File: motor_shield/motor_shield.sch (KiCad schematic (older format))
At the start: 22 parts, among them J1 Screw_Terminal_01x02, J2 Screw_Terminal_01x02, J3 Screw_Terminal_01x02, J4 Conn_01x04, J5 Conn_01x04, J6 Conn_01x04, U1 DRV8834_CARRIER, U10 SHARP_GP2Y0A21YK0F, U11 SHARP_GP2Y0A21YK0F, U2 DRV8834_CARRIER, U3 DRV8834_CARRIER, U4 ARDUINO_MICRO, U5 RASPBERRY_PI, U6 SHARP_GP2Y0A21YK0F, U7 SHARP_GP2Y0A21YK0F, U8 SHARP_GP2Y0A21YK0F, U9 SHARP_GP2Y0A21YK0F

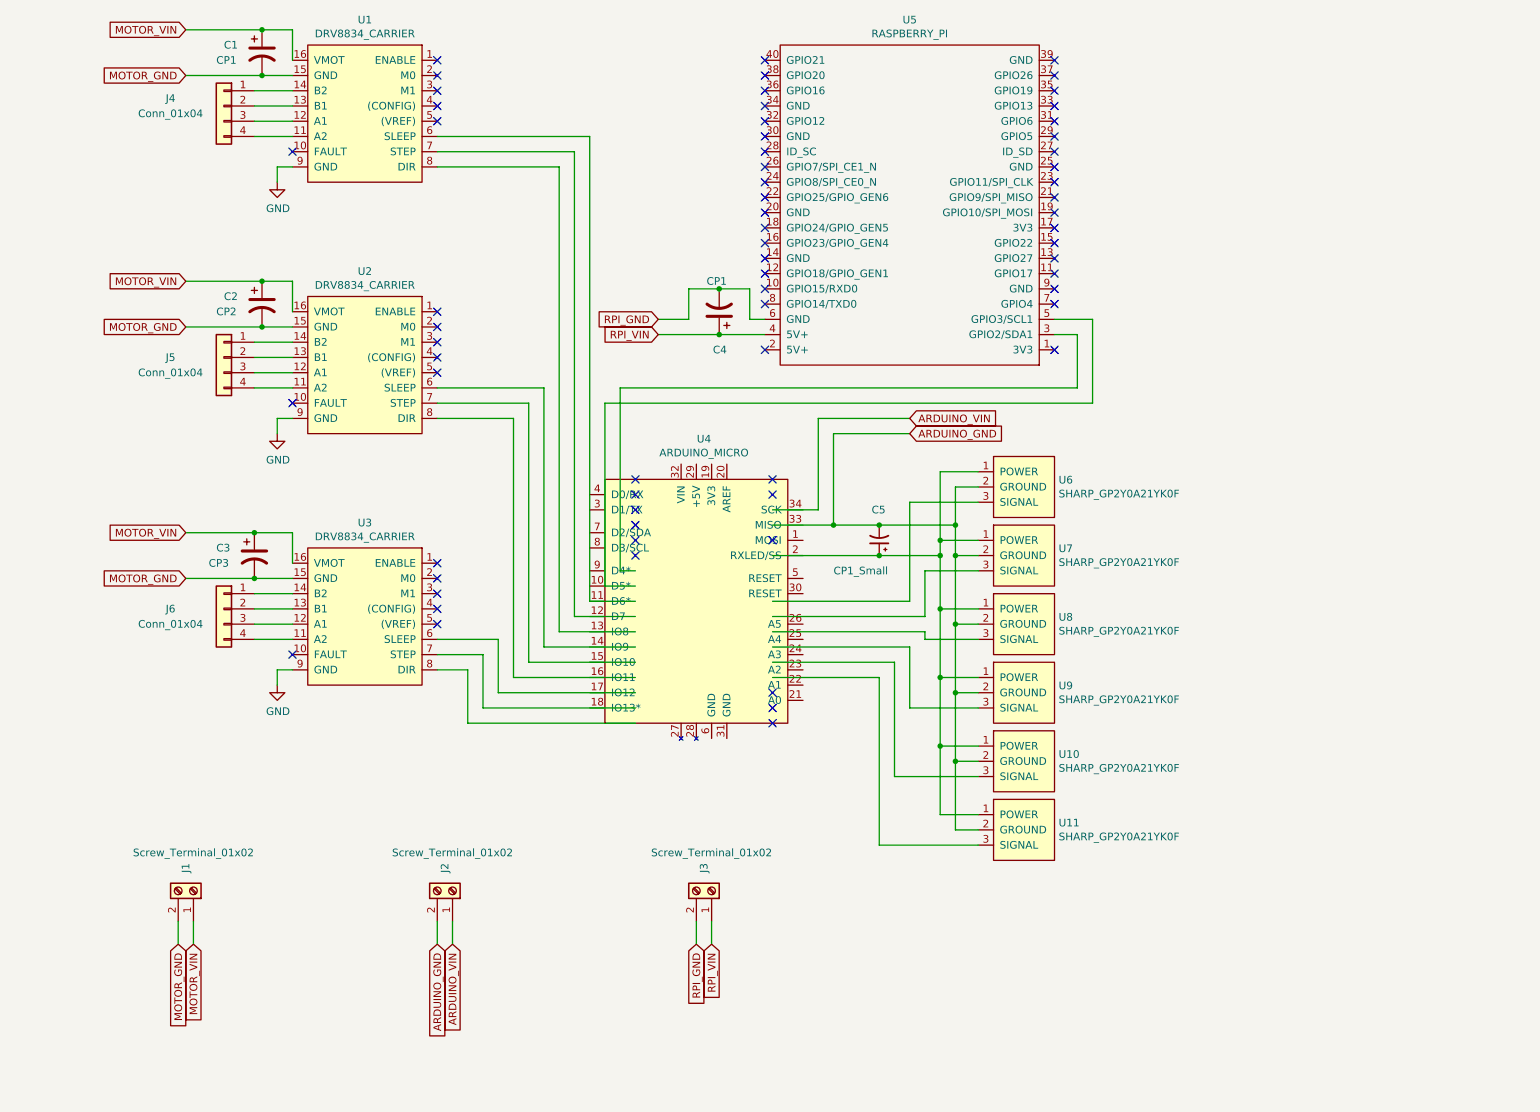
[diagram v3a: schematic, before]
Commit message: Continued work on motor shield
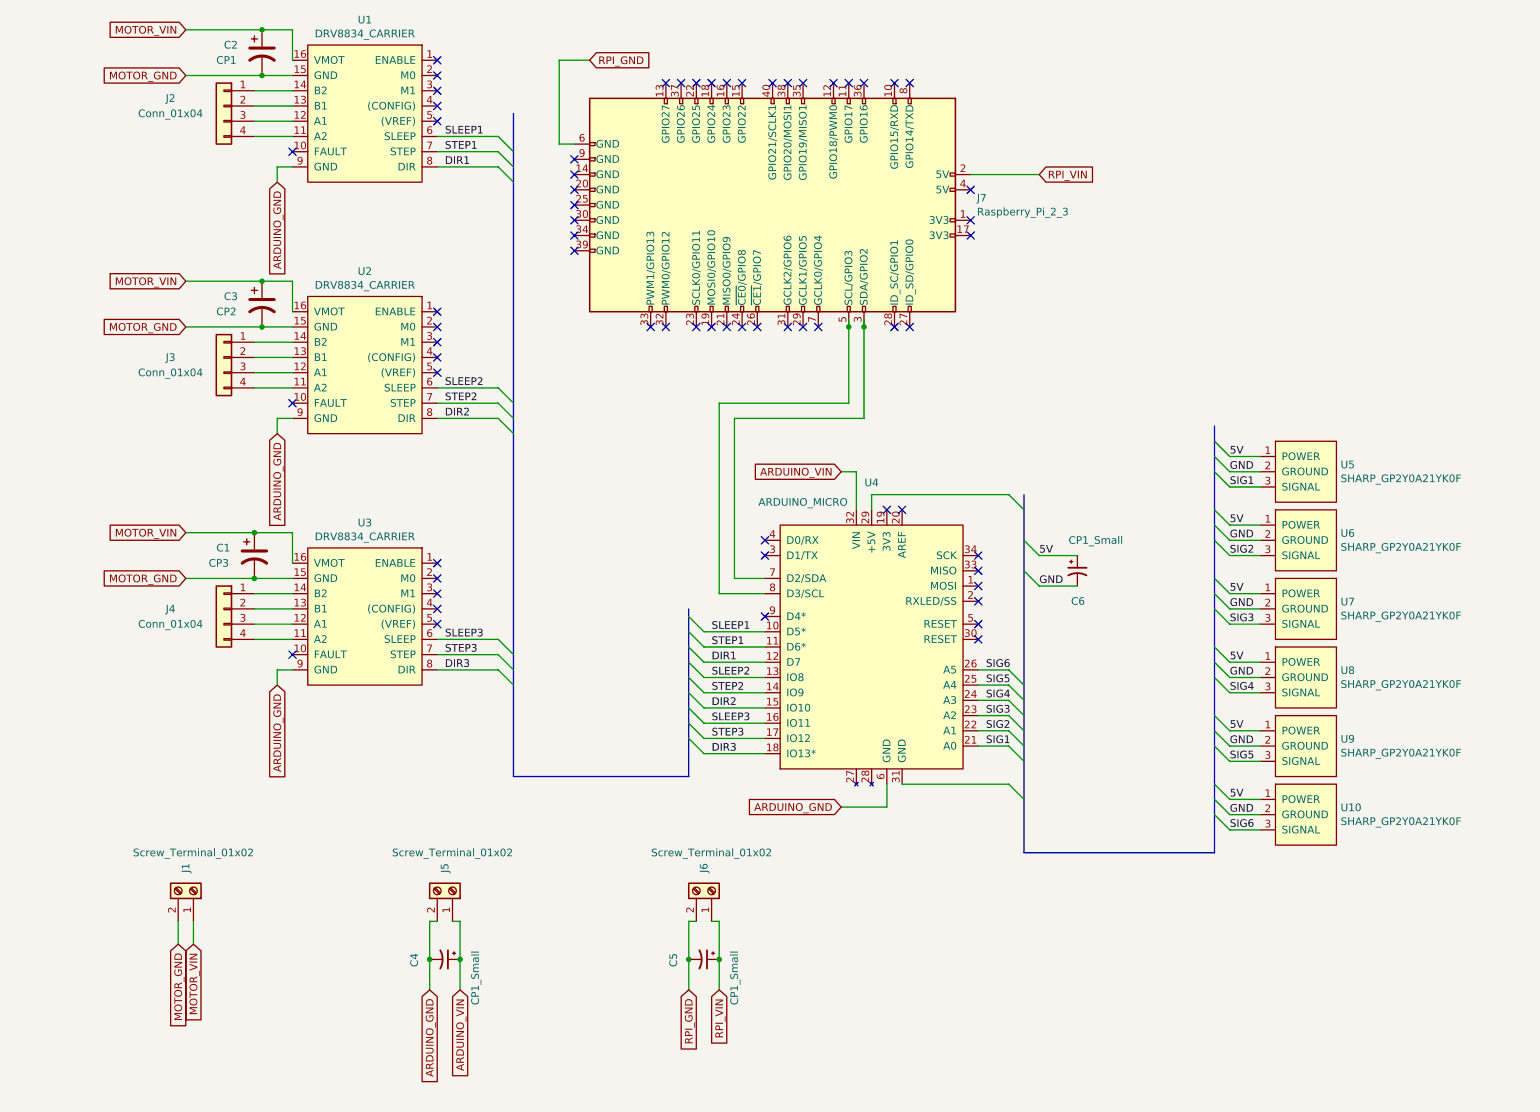
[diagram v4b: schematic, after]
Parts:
- removed C4: CP1, Capacitor_THT:CP_Radial_D8.0mm_P2.50mm, symbol Device:CP1
- removed U5: RASPBERRY_PI, Connector_PinHeader_2.54mm:PinHeader_2x20_P2.54mm_Vertical, symbol CATPOO:RASPBERRY_PI
- added C5, C6: CP1_Small, Capacitor_THT:CP_Radial_D5.0mm_P2.50mm, symbol Device:CP1_Small
- added J7: Raspberry_Pi_2_3, Connector_PinHeader_2.54mm:PinHeader_2x20_P2.54mm_Vertical, symbol Connector:Raspberry_Pi_2_3
- renumbered C3 to C1, C1 to C2, C2 to C3, C5 to C4, J4 to J2, J5 to J3, J6 to J4, J2 to J5, J3 to J6, U11 to U10, U6 to U5, U7 to U6, U8 to U7, U9 to U8, U10 to U9
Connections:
- net labels added: 5V, DIR1, DIR2, DIR3, SIG1, SIG2, SIG3, SIG4, SIG5, SIG6, SLEEP1, SLEEP2, SLEEP3, STEP1, STEP2, STEP3
- wire segments 136 -> 112
- no-connect marks 66 -> 65
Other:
- moved on the sheet: C4, U10, U5, U6, U7, U8, U9

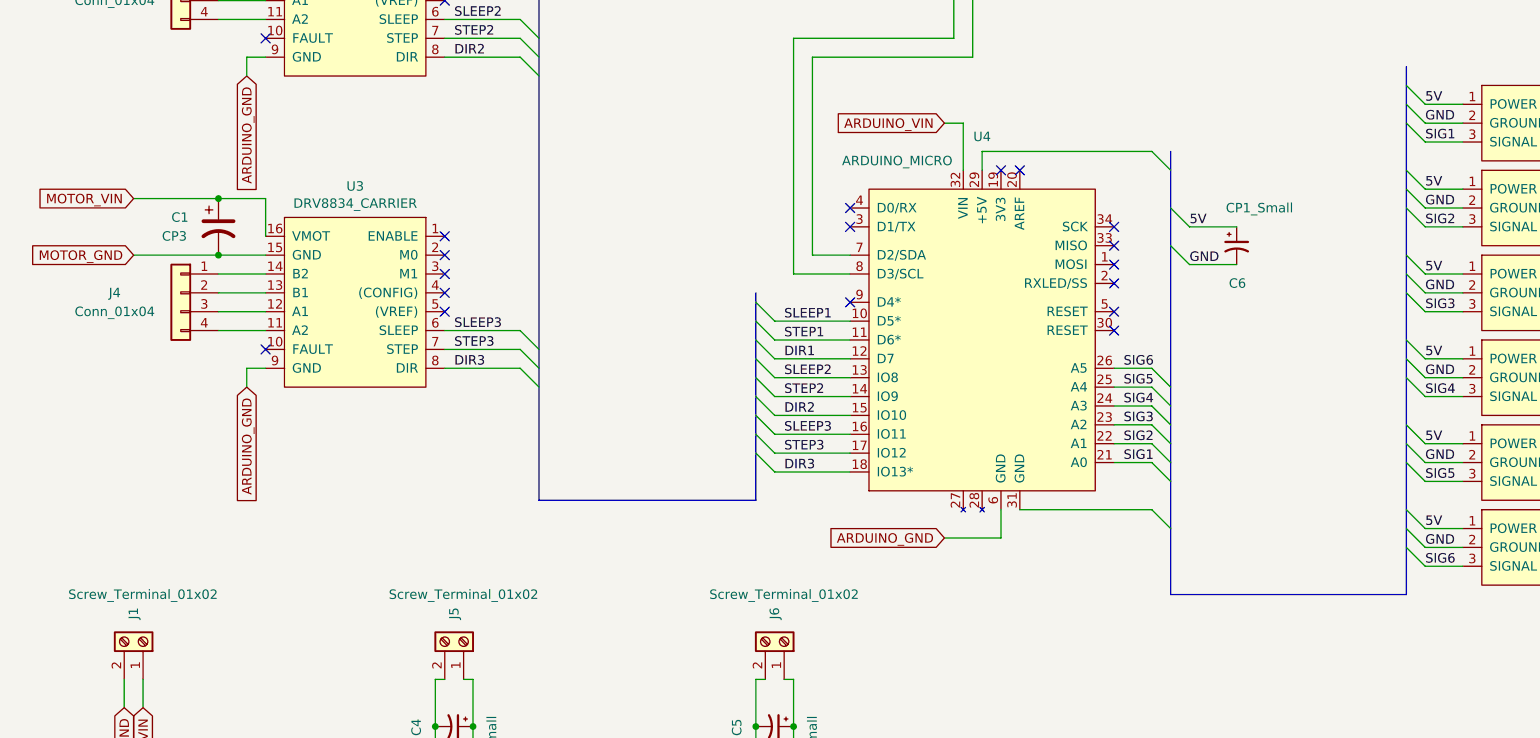
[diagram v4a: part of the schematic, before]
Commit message: Fix mobo schematic
flipped the order of dir, step, sleep to make it easier to route wires
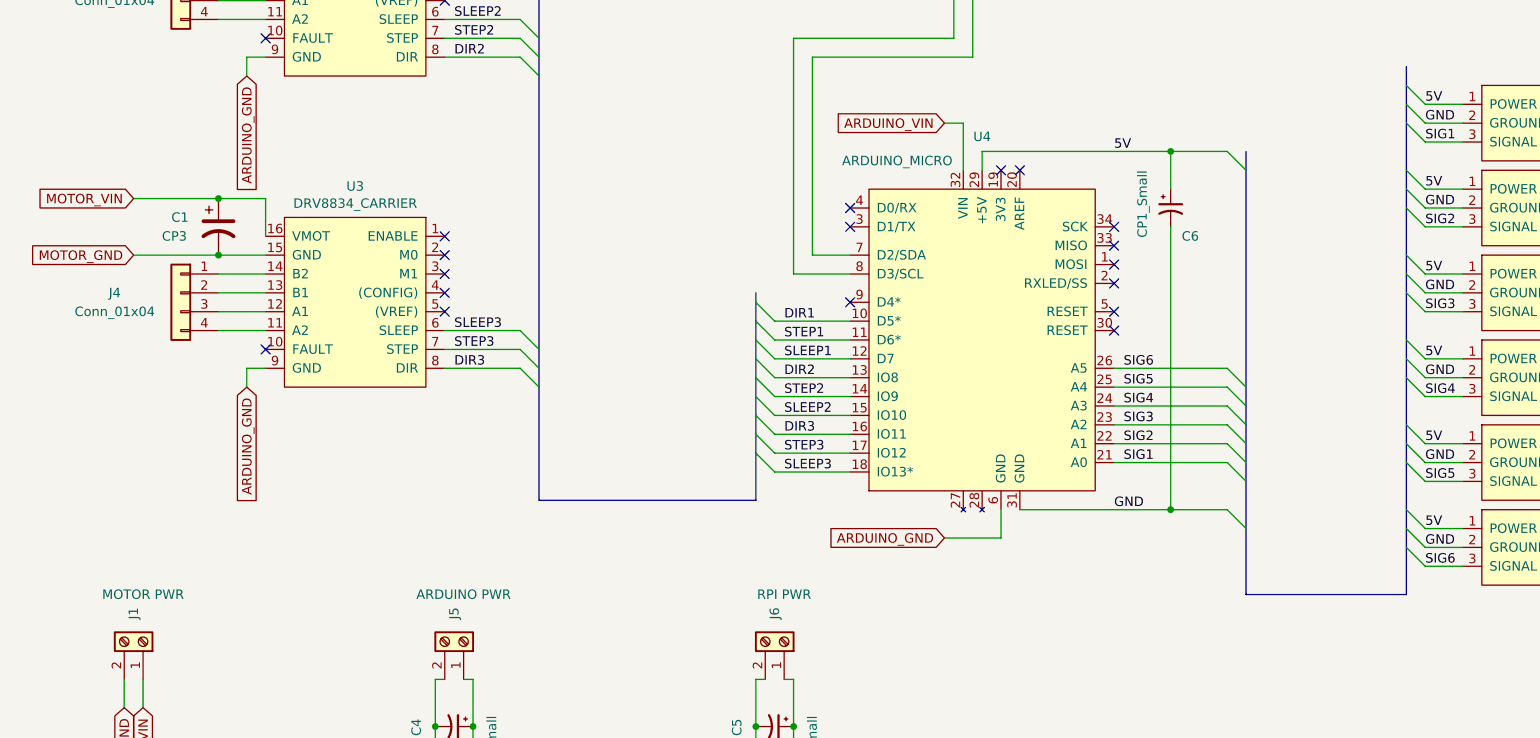
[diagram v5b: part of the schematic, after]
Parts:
- J1: value Screw_Terminal_01x02 -> MOTOR PWR
- J5: value Screw_Terminal_01x02 -> ARDUINO PWR
- J6: value Screw_Terminal_01x02 -> RPI PWR
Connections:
- net 5V: now also U4.29 (+5V)
- net DIR1: now also U4.10 (D5*); no longer U4.12 (D7)
- net DIR2: now also U4.13 (IO8); no longer U4.15 (IO10)
- net DIR3: now also U4.16 (IO11); no longer U4.18 (IO13*)
- net GND: now also U4.31 (GND)
- net SLEEP1: now also U4.12 (D7); no longer U4.10 (D5*)
- net SLEEP2: now also U4.15 (IO10); no longer U4.13 (IO8)
- net SLEEP3: now also U4.18 (IO13*); no longer U4.16 (IO11)
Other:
- moved on the sheet: C6
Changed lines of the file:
@@
 P 1400 6450
 F 0 "J1" H 1550 6400 50  0000 C CNN
-F 1 "Screw_Terminal_01x02" V 1650 6450 50  0000 C CNN
+F 1 "MOTOR PWR" V 1650 6450 50  0000 C CNN
 F 2 "CATPOO:TerminalBlock_Pololu-2_P5.00mm" H 1400 6450 50  0001 C CNN
 F 3 "~" H 1400 6450 50  0001 C CNN
@@
 	1    0    0    -1
 $EndComp
-$Comp
-L Device:CP1_Small C4
-U 1 1 5C9E9E39
-P 3050 6900
-F 0 "C4" H 3100 6700 50  0000 R CNN
-F 1 "CP1_Small" H 3350 7100 50  0000 R CNN
-F 2 "Capacitor_THT:CP_Radial_D5.0mm_P2.50mm" H 3050 6900 50  0001 C CNN
-F 3 "~" H 3050 6900 50  0001 C CNN
-	1    3050 6900
-	0    1    1    0
-$EndComp
 Wire Wire Line
 	2050 5000 1950 5000
@@
 P 3100 6450
 F 0 "J5" H 3250 6400 50  0000 C CNN
-F 1 "Screw_Terminal_01x02" V 3350 6450 50  0000 C CNN
+F 1 "ARDUINO PWR" V 3350 6450 50  0000 C CNN
 F 2 "CATPOO:TerminalBlock_Pololu-2_P5.00mm" H 3100 6450 50  0001 C CNN
 F 3 "~" H 3100 6450 50  0001 C CNN
@@
 P 4800 6450
 F 0 "J6" H 4950 6400 50  0000 C CNN
-F 1 "Screw_Terminal_01x02" V 5050 6450 50  0000 C CNN
+F 1 "RPI PWR" V 5050 6450 50  0000 C CNN
 F 2 "CATPOO:TerminalBlock_Pololu-2_P5.00mm" H 4800 6450 50  0001 C CNN
 F 3 "~" H 4800 6450 50  0001 C CNN
@@
 	3000 6650 2950 6650
 Wire Wire Line
-	2950 6650 2950 6900
-Wire Wire Line
-	3150 6900 3150 6650
-Wire Wire Line
 	3150 6650 3100 6650
-Wire Wire Line
-	3150 6900 3150 7100
-Connection ~ 3150 6900
-Wire Wire Line
-	2950 7100 2950 6900
-Connection ~ 2950 6900
 $Comp
 L CATPOO:ARDUINO_MICRO U4
@@
 Wire Wire Line
 	5750 3950 5750 3700
-Wire Wire Line
-	5750 3700 5650 3700
-Entry Wire Line
-	6750 5500 6850 5600
-Entry Wire Line
-	6750 5400 6850 5500
-Entry Wire Line
-	6750 5300 6850 5400
-Entry Wire Line
-	6750 5200 6850 5300
-Entry Wire Line
-	6750 5100 6850 5200
-Entry Wire Line
-	6750 5000 6850 5100
-Entry Wire Line
-	6750 3850 6850 3950
-Entry Wire Line
-	6750 5750 6850 5850
+Entry Wire Line
+	7150 5500 7250 5600
+Entry Wire Line
+	7150 5400 7250 5500
+Entry Wire Line
+	7150 5300 7250 5400
+Entry Wire Line
+	7150 5200 7250 5300
+Entry Wire Line
+	7150 5100 7250 5200
+Entry Wire Line
+	7150 5000 7250 5100
+Entry Wire Line
+	7150 3850 7250 3950
+Entry Wire Line
+	7150 5750 7250 5850
 Wire Wire Line
 	5950 5750 5950 5900
@@
 	5950 5900 5650 5900
 Wire Wire Line
-	6750 5750 6050 5750
-Wire Wire Line
-	6750 5500 6550 5500
-Wire Wire Line
-	6550 5400 6750 5400
-Wire Wire Line
-	6750 5300 6550 5300
-Wire Wire Line
-	6550 5200 6750 5200
-Wire Wire Line
-	6750 5100 6550 5100
-Wire Wire Line
-	6550 5000 6750 5000
+	7150 5750 6850 5750
+Wire Wire Line
+	7150 5500 6550 5500
+Wire Wire Line
+	6550 5400 7150 5400
+Wire Wire Line
+	7150 5300 6550 5300
+Wire Wire Line
+	6550 5200 7150 5200
+Wire Wire Line
+	7150 5100 6550 5100
+Wire Wire Line
+	6550 5000 7150 5000
 Wire Wire Line
 	5850 3850 5850 3950
 Wire Bus Line
-	6850 6200 8100 6200
+	7250 6200 8100 6200
 Entry Wire Line
 	8100 3500 8200 3600
@@
 	5150 5550 4750 5550
 Text Label 4800 5350 0    50   ~ 0
-SLEEP3
+DIR3
 Text Label 4800 5450 0    50   ~ 0
 STEP3
 Text Label 4800 5550 0    50   ~ 0
-DIR3
+SLEEP3
 Wire Wire Line
 	5150 5050 4750 5050
@@
 	5150 5250 4750 5250
 Text Label 4800 5050 0    50   ~ 0
-SLEEP2
+DIR2
 Text Label 4800 5150 0    50   ~ 0
 STEP2
 Text Label 4800 5250 0    50   ~ 0
-DIR2
+SLEEP2
 Wire Wire Line
 	5150 4750 4750 4750
@@
 	5150 4950 4750 4950
 Text Label 4800 4750 0    50   ~ 0
-SLEEP1
+DIR1
 Text Label 4800 4850 0    50   ~ 0
 STEP1
 Text Label 4800 4950 0    50   ~ 0
-DIR1
+SLEEP1
 Wire Wire Line
 	5800 2700 5800 2750
 Wire Wire Line
 	5800 3350 4950 3350
-Wire Wire Line
-	4950 3350 4950 4400
 Wire Wire Line
 	4950 4400 5150 4400
@@
 	5800 2750 5800 3350
 Wire Wire Line
-	6750 3850 5850 3850
-Entry Wire Line
-	6850 4150 6950 4250
-Entry Wire Line
-	6850 4350 6950 4450
+	7150 3850 6850 3850
 $Comp
 L Device:CP1_Small C6
 U 1 1 5CA45096
-P 7200 4350
-F 0 "C6" H 7250 4150 50  0000 R CNN
-F 1 "CP1_Small" H 7500 4550 50  0000 R CNN
-F 2 "Capacitor_THT:CP_Radial_D5.0mm_P2.50mm" H 7200 4350 50  0001 C CNN
-F 3 "~" H 7200 4350 50  0001 C CNN
-	1    7200 4350
-	1    0    0    -1
-$EndComp
-Wire Wire Line
-	6950 4250 7200 4250
-Wire Wire Line
-	7200 4450 6950 4450
+P 6850 4150
+F 0 "C6" H 7000 4000 50  0000 R CNN
+F 1 "CP1_Small" V 6700 4350 50  0000 R CNN
+F 2 "Capacitor_THT:CP_Radial_D5.0mm_P2.50mm" H 6850 4150 50  0001 C CNN
+F 3 "~" H 6850 4150 50  0001 C CNN
+	1    6850 4150
+	1    0    0    -1
+$EndComp
+Text Label 6550 3850 0    50   ~ 0
+5V
+Text Label 6550 5750 0    50   ~ 0
+GND
+$Comp
+L Device:CP1_Small C4
+U 1 1 5C9E9E39
+P 3050 6900
+F 0 "C4" H 3100 6700 50  0000 R CNN
+F 1 "CP1_Small" H 3350 7100 50  0000 R CNN
+F 2 "Capacitor_THT:CP_Radial_D5.0mm_P2.50mm" H 3050 6900 50  0001 C CNN
+F 3 "~" H 3050 6900 50  0001 C CNN
+	1    3050 6900
+	0    1    1    0
+$EndComp
+Wire Wire Line
+	4950 3350 4950 4400
+Wire Wire Line
+	5750 3700 5650 3700
+Wire Wire Line
+	3150 6900 3150 6650
+Wire Wire Line
+	3150 6900 3150 7100
+Connection ~ 3150 6900
+Wire Wire Line
+	2950 6650 2950 6900
+Wire Wire Line
+	2950 7100 2950 6900
+Connection ~ 2950 6900
+Wire Wire Line
+	6850 4050 6850 3850
+Connection ~ 6850 3850
+Wire Wire Line
+	6850 3850 5850 3850
+Wire Wire Line
+	6850 4250 6850 5750
+Connection ~ 6850 5750
+Wire Wire Line
+	6850 5750 6050 5750
 Wire Bus Line
 	3500 1350 3500 5700
 Wire Bus Line
-	6850 3850 6850 6200
+	7250 3850 7250 6200
 Wire Bus Line
 	4650 4600 4650 5700
 Wire Bus Line
 	8100 3400 8100 6200
-Text Label 6950 4450 0    50   ~ 0
-GND
-Text Label 6950 4250 0    50   ~ 0
-5V
 $EndSCHEMATC

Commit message: Finish circuit board design
off to oshpark!
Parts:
- removed J1: MOTOR PWR, CATPOO:TerminalBlock_Pololu-2_P5.00mm, symbol Connector:Screw_Terminal_01x02
- added D1: 1N4001, Diode_THT:D_DO-41_SOD81_P10.16mm_Horizontal, symbol Diode:1N4001
- J5: value ARDUINO PWR -> MOTOR PWR
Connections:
- net GND is gone; now on net MOTOR_GND: C6.2, U10.2 (GROUND), U4.31 (GND), U5.2 (GROUND), U6.2 (GROUND), U7.2 (GROUND), U8.2 (GROUND), U9.2 (GROUND)
- net ARDUINO_GND: no longer C4.2, J5.2 (Pin_2), U4.6 (GND)
- net MOTOR_GND: now also C4.2, J5.2 (Pin_2)
- net MOTOR_VIN: now also J5.1 (Pin_1), D1.2 (A)
- net SDA: now reaches J7.3 (SDA/GPIO2), U4.7 (D2/SDA)
- net SCL: now reaches J7.5 (SCL/GPIO3), U4.8 (D3/SCL)
- net ARDUINO_VIN: no longer names the net of C4.1, U4.32 (VIN)
- net ARDUINO_VIN: now also D1.1 (K); no longer J5.1 (Pin_1)
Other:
- moved on the sheet: C4, C6
